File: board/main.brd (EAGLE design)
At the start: 91 x 76 mm, 53 parts, among them IC2 L6387EDIP8, IC3 L6387EDIP8, IC4 L6387EDIP8, J3 FUSE

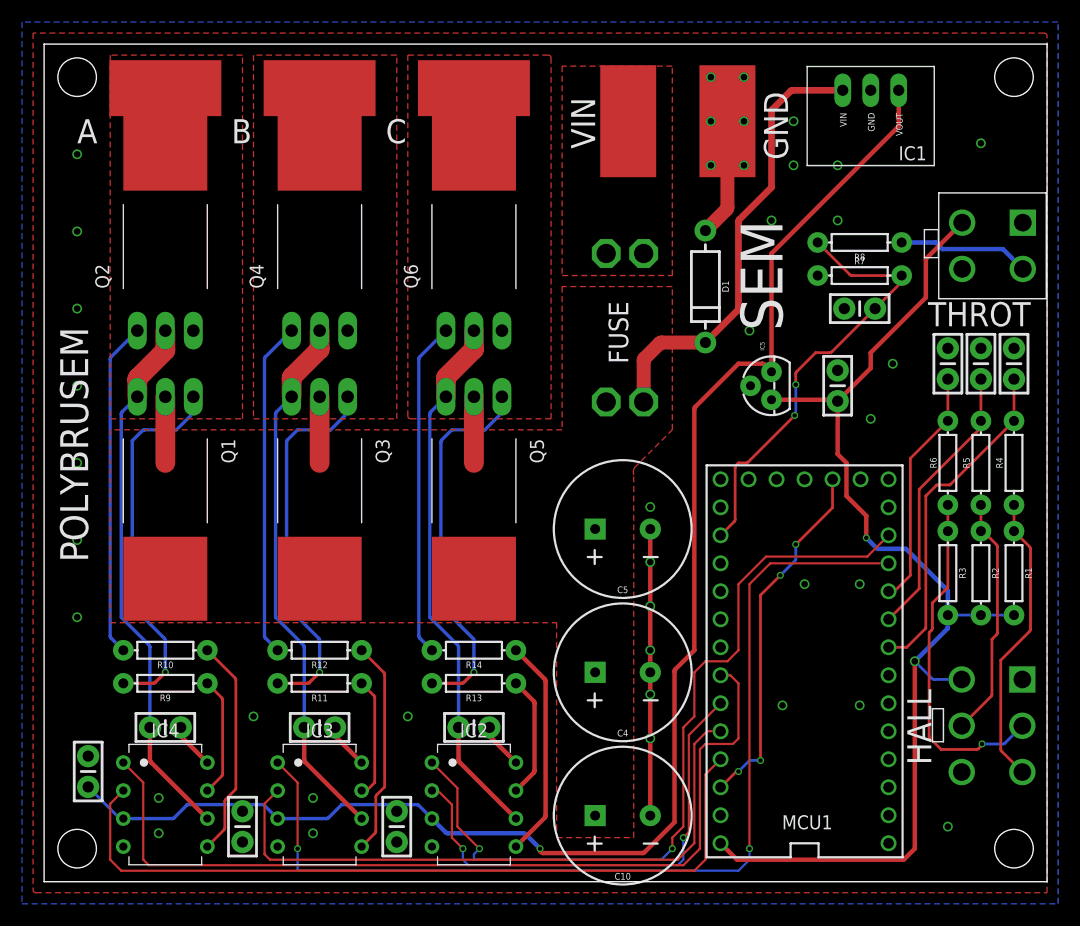
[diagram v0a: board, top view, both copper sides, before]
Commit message: Flipped connectors, changed silkscreen
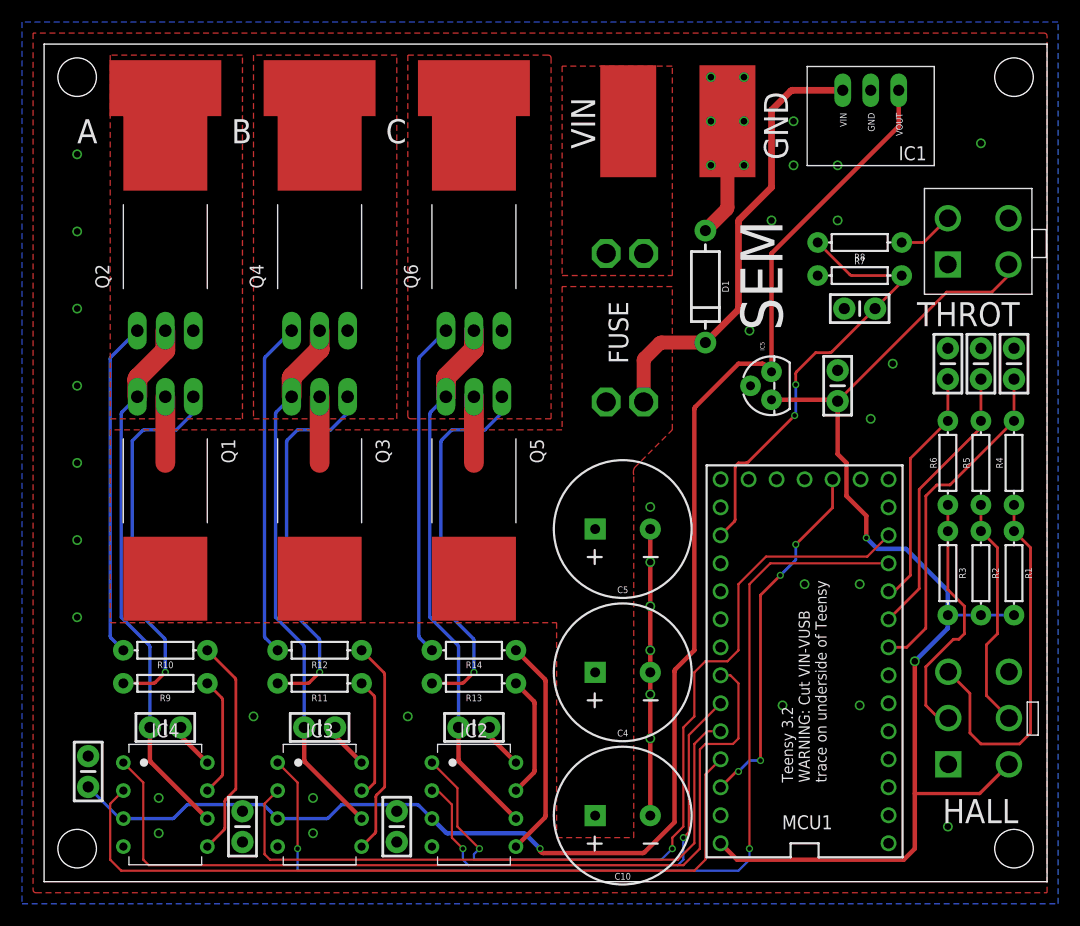
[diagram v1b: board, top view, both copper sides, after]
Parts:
- moved U$1 5.66 mm to (87.5, 56.0), turned to 90 degrees
- moved U$2 5.06 mm to (85.0, 17.0), turned to 90 degrees
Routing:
- net N$2: track 31.6 -> 23.1 mm, vias 1 -> 0
- net N$6: track 26.7 -> 34.0 mm
- net N$7: track 12.0 -> 5.10 mm
- net 5V: track 104.0 -> 109.1 mm
- net N$4: track 22.1 -> 21.2 mm
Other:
- board text added: "EasyController2 Designed by PLG, March 2019"
- board text added: "Teensy 3.2 WARNING: Cut VIN-VUSB trace on underside of Teensy"
- board text removed: "BLDC Controller 1.1 Designed by PLG, Feb 2019 POLYBRUSEM, Shell Eco-Marathon"
- board text removed: "POLYBRUSEM"
